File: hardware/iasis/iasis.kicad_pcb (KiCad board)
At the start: 6 copper layers, 130 x 100 mm, 658 parts, among them J1001 USB4105-GF-A-120, J1101 TSW-104-07-G-D, J1131 SM04B-SRSS-TB, J1132 UART debug, J401 1054500101, J501 1054500101, J601 1054500101, J701 1054500101, J801 1054500101, J901 1054500101, Q1001 CSD18543Q3A, Q1002 CSD18543Q3A, Q1221 2N7002, Q1230 2N7002, Q1231 2N7002, Q1232 2N7002, Q1321 2N7002, Q1330 2N7002, Q1331 2N7002, Q1332 2N7002, Q1421 2N7002, Q1430 2N7002, Q1431 2N7002, Q1432 2N7002, Q1521 2N7002, Q1530 2N7002, Q1531 2N7002, Q1532 2N7002, Q1621 2N7002, Q1630 2N7002, Q1631 2N7002, Q1632 2N7002, Q1911 2N7002, Q1912 2N7002, SW1101 PTS645SL50SMTR92LFS, SW1102 PTS645SL50SMTR92LFS, SW1171 PTS645SL50SMTR92LFS, U1001 LM74502DDFR, U1002 CH224Q, U1003 TPS26600PWPR, U1040 AP3441SHE-7B, U1060 AP3441SHE-7B, U1080 TPS3808G33DBVR, U1101 RP2354B, U1131 TCA9548APWR, U1141 TMUX1511PWR, U1142 TMUX1511PWR, U1171 SN74AHCT1G125DBVR, U1172 TCA6408ARGTR, U1181 74HC595D,118, U1182 74HC595D,118, U1202 TPS259470LRPWR, U1203 74LVC2G08DC-Q100H, U1230 LMR51450SDRRR, U1231 TPS26600PWPR, U1232 LM4040DIM3X-2.5/NOPB, U1302 TPS259470LRPWR, U1303 74LVC2G08DC-Q100H, U1330 LMR51450SDRRR, U1331 TPS26600PWPR, U1332 LM4040DIM3X-2.5/NOPB, U1402 TPS259470LRPWR, U1403 74LVC2G08DC-Q100H, U1430 LMR51450SDRRR, U1431 TPS26600PWPR, U1432 LM4040DIM3X-2.5/NOPB, U1502 TPS259470LRPWR, U1503 74LVC2G08DC-Q100H, U1530 LMR51450SDRRR, U1531 TPS26600PWPR, U1532 LM4040DIM3X-2.5/NOPB, U1602 TPS259470LRPWR, U1603 74LVC2G08DC-Q100H, U1630 LMR51450SDRRR, U1631 TPS26600PWPR, U1632 LM4040DIM3X-2.5/NOPB, U1901 AP22653W6-7, U1902 TPS259470LRPWR, U201 USB7206CT/KDX, U204 SN74AUP1G08DCKR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

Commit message: Use smaller charge inductors and bulk capacitors, and solder pads for debug
The 6.8 uH PSTMAA666460 (12.5 A saturation) replaces the 10 uH 11 x 10 mm
inductor, a 6.3 mm 35 V hybrid capacitor the 10 mm 50 V bulk capacitor on
each charging buck, and an 8 mm 68 uF part the 100 uF on the charging input.
SWD and UART become three solder pads each in Raspberry Pi debug order.
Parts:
- C1002: value 100u 50V -> 68u 50V; footprint Capacitor_SMD:CP_Elec_10x10.5 -> Capacitor_SMD:CP_Elec_8x10.5
- C1234, C1334, C1434, C1534, C1634: value 100u 50V -> 100u 35V; footprint Capacitor_SMD:CP_Elec_10x10.5 -> Capacitor_SMD:CP_Elec_6.3x7.7
- J1101: value TSW-104-07-G-D -> SWD debug; footprint Connector_PinHeader_2.54mm:PinHeader_2x04_P2.54mm_Vertical -> Iasis:SolderPads_1x03_P2.54mm
- J1132: footprint Connector_PinHeader_2.54mm:PinHeader_1x03_P2.54mm_Vertical -> Iasis:SolderPads_1x03_P2.54mm
- L1230, L1330, L1430, L1530, L1630: value 10u 10A -> 6.8u 12.5A; footprint Iasis:PSPMAA1040 -> Iasis:PSTMAA666460
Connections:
- J1101 pad 1: 3V3_AON -> /RP2354 controller/MCU_SWCLK
- J1101 pad 2: /RP2354 controller/MCU_SWDIO -> GND
- J1101 pad 3: GND -> /RP2354 controller/MCU_SWDIO
- J1132 pad 1: GND -> MCU_UART_RX
- J1132 pad 2: MCU_UART_TX -> GND
- J1132 pad 3: MCU_UART_RX -> MCU_UART_TX

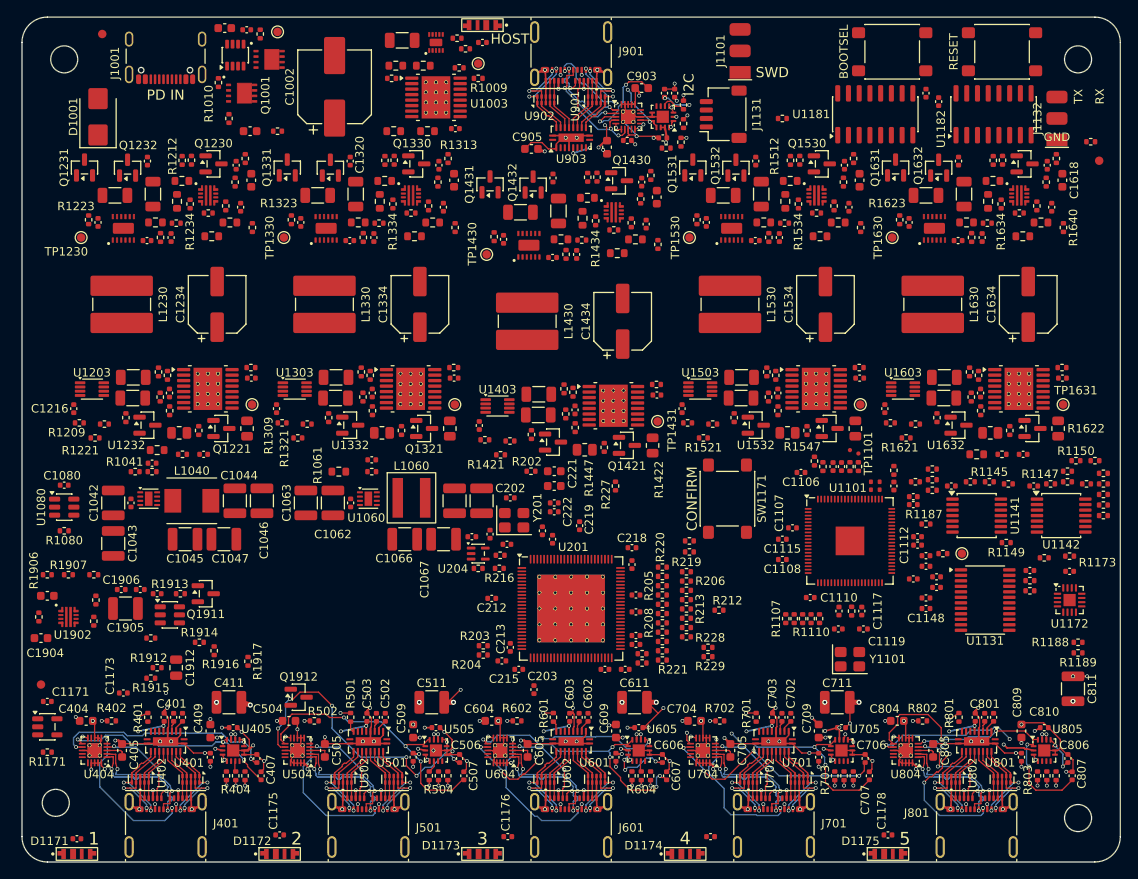
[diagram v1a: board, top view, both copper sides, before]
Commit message: Place the board on a 125 × 89 mm outline
Rear: PD input, host port, shift registers and expander, recovery
buttons, debug pads and the I2C socket. Five identical charge cells
span the board, with the host lanes in the gap between cells 2 and 3.
Middle: logic bucks and host power, hub, controller and port sense.
Target data cells keep their routing; everything else is unrouted.
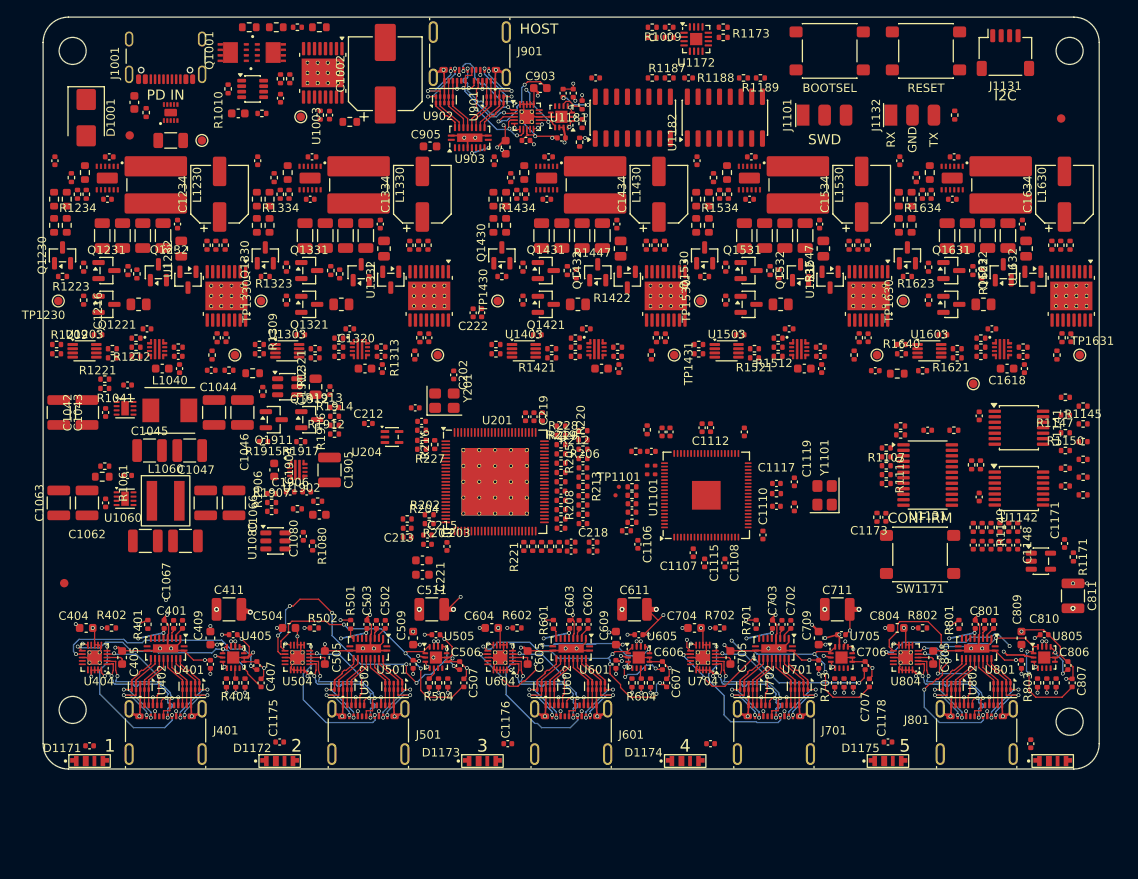
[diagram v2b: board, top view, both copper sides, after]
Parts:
- moved R1171 123.6 mm to (174.4, 113.9), turned to 90 degrees
- moved C1171 121.8 mm to (173.4, 112.3), turned to 90 degrees
- moved U1171 119.2 mm to (170.6, 114.4)
- moved D1170 110.2 mm to (172.0, 138.1), turned to 0 degrees
- moved C1170 105.4 mm to (169.4, 136.0), turned to 90 degrees
- moved C1173 92.6 mm to (152.2, 109.2), turned to 90 degrees
- moved R1181 87.1 mm to (151.2, 109.2), turned to 90 degrees
- moved C1172 80.0 mm to (126.6, 51.2)
- moved U1172 79.8 mm to (129.8, 52.6)
- moved R1189 77.7 mm to (137.4, 57.2)
- moved R1188 77.7 mm to (135.4, 57.2)
- moved R1172 75.9 mm to (126.6, 52.4)
- moved R1173 74.8 mm to (133.0, 51.2)
- moved R1187 60.9 mm to (126.6, 57.2)
- moved C1065 40.1 mm to (64.6, 112.0), turned to 0 degrees
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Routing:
- net GND: track 255.9 -> 250.6 mm
- net 3V3_AON: track 69.1 -> 67.9 mm, vias 71 -> 70
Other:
- board size 130 x 100 mm -> 125 x 89 mm
